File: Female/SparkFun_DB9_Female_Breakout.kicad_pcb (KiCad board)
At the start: 4 copper layers, 22.9 x 31 mm, 23 parts, among them J1 DB9-Female, J2 Conn_01x09

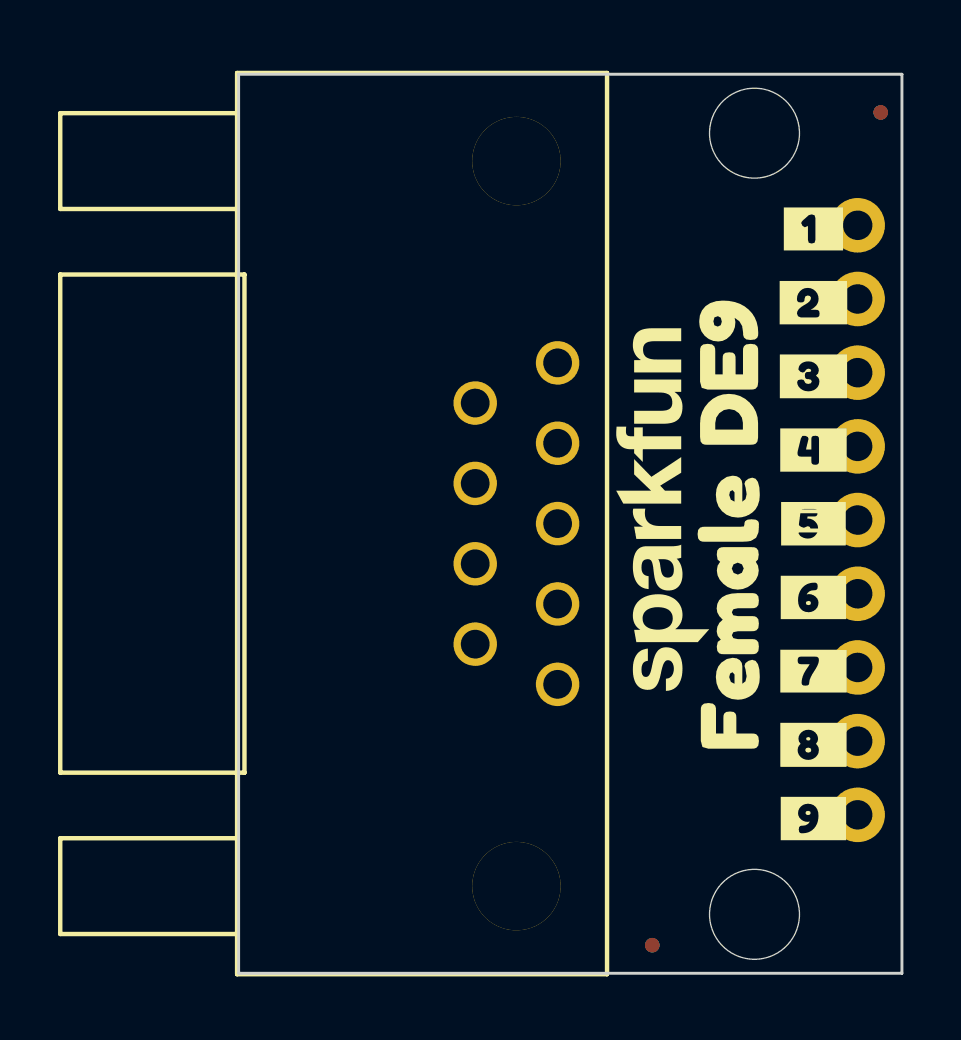
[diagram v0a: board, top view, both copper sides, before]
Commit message: Adds a male footprint for the DB9 and updates the affected board
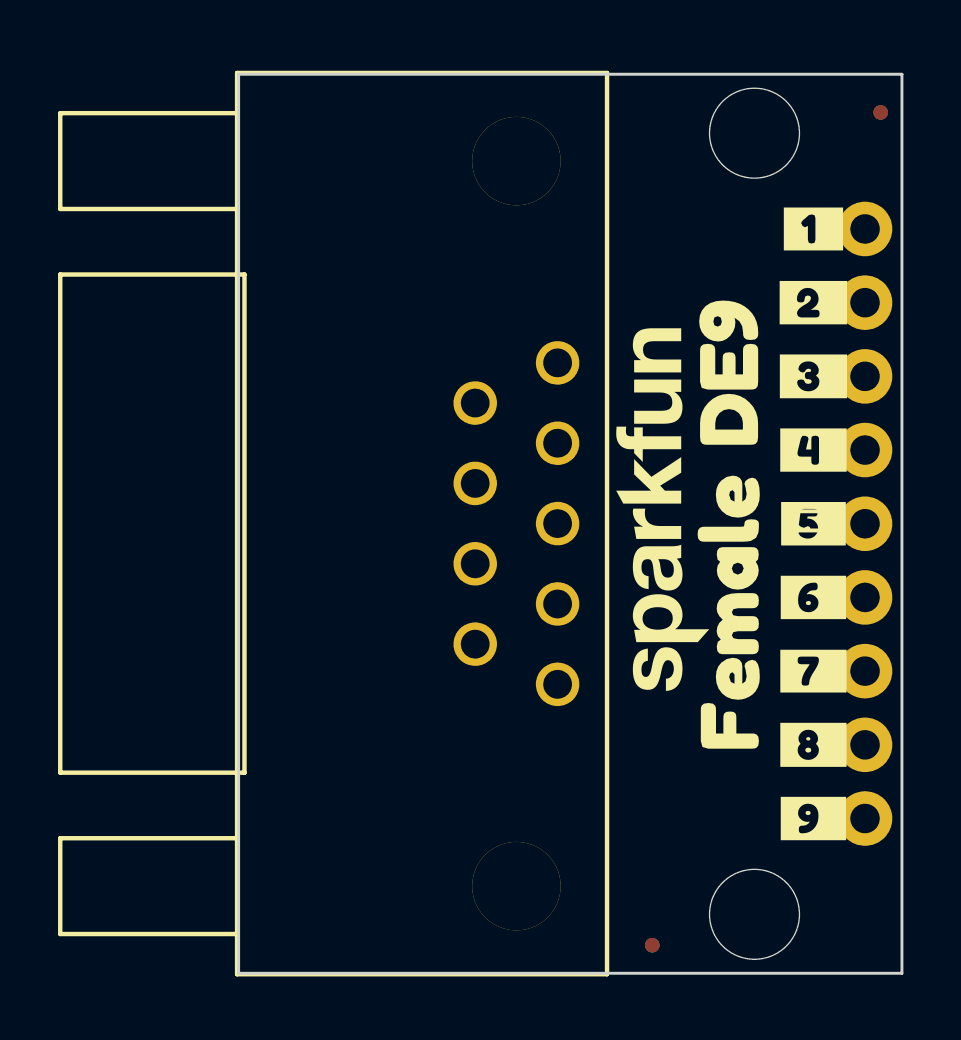
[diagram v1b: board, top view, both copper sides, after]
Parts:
- moved J2 20.2 mm to (131.1, 98.6), turned to -90 degrees
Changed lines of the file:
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@@
 	(footprint "SparkFun-Connector:1x09"
 		(layer "B.Cu")
-		(at 130.81 118.745 90)
+		(at 131.064 98.552 -90)
 		(tags "SparkFun")
 		(property "Reference" "J2"
@@
 		)
 		(property "Datasheet" ""
-			(at 0 0 270)
+			(at 0 0 90)
 			(unlocked yes)
 			(layer "B.Fab")
@@
 		)
 		(property "Description" "Basic 0.1\" PTH"
-			(at 0 0 270)
+			(at 0 0 90)
 			(unlocked yes)
 			(layer "B.Fab")
@@
 		(fp_poly
 			(pts
+				(xy -0.254 -0.254) (xy 0.254 -0.254) (xy 0.254 0.254) (xy -0.254 0.254)
+			)
+			(stroke
+				(width 0)
+				(type default)
+			)
+			(fill yes)
+			(layer "B.Fab")
+		)
+		(fp_poly
+			(pts
+				(xy 2.286 -0.254) (xy 2.794 -0.254) (xy 2.794 0.254) (xy 2.286 0.254)
+			)
+			(stroke
+				(width 0)
+				(type default)
+			)
+			(fill yes)
+			(layer "B.Fab")
+		)
+		(fp_poly
+			(pts
+				(xy 4.826 -0.254) (xy 5.334 -0.254) (xy 5.334 0.254) (xy 4.826 0.254)
+			)
+			(stroke
+				(width 0)
+				(type default)
+			)
+			(fill yes)
+			(layer "B.Fab")
+		)
+		(fp_poly
+			(pts
+				(xy 7.366 -0.254) (xy 7.874 -0.254) (xy 7.874 0.254) (xy 7.366 0.254)
+			)
+			(stroke
+				(width 0)
+				(type default)
+			)
+			(fill yes)
+			(layer "B.Fab")
+		)
+		(fp_poly
+			(pts
+				(xy 9.906 -0.254) (xy 10.414 -0.254) (xy 10.414 0.254) (xy 9.906 0.254)
+			)
+			(stroke
+				(width 0)
+				(type default)
+			)
+			(fill yes)
+			(layer "B.Fab")
+		)
+		(fp_poly
+			(pts
+				(xy 12.446 -0.254) (xy 12.954 -0.254) (xy 12.954 0.254) (xy 12.446 0.254)
+			)
+			(stroke
+				(width 0)
+				(type default)
+			)
+			(fill yes)
+			(layer "B.Fab")
+		)
+		(fp_poly
+			(pts
+				(xy 14.986 -0.254) (xy 15.494 -0.254) (xy 15.494 0.254) (xy 14.986 0.254)
+			)
+			(stroke
+				(width 0)
+				(type default)
+			)
+			(fill yes)
+			(layer "B.Fab")
+		)
+		(fp_poly
+			(pts
+				(xy 17.526 -0.254) (xy 18.034 -0.254) (xy 18.034 0.254) (xy 17.526 0.254)
+			)
+			(stroke
+				(width 0)
+				(type default)
+			)
+			(fill yes)
+			(layer "B.Fab")
+		)
+		(fp_poly
+			(pts
 				(xy 20.066 -0.254) (xy 20.574 -0.254) (xy 20.574 0.254) (xy 20.066 0.254)
 			)
@@
 			(layer "B.Fab")
 		)
-		(fp_poly
-			(pts
-				(xy 17.526 -0.254) (xy 18.034 -0.254) (xy 18.034 0.254) (xy 17.526 0.254)
-			)
-			(stroke
-				(width 0)
-				(type default)
-			)
-			(fill yes)
-			(layer "B.Fab")
-		)
-		(fp_poly
-			(pts
-				(xy 14.986 -0.254) (xy 15.494 -0.254) (xy 15.494 0.254) (xy 14.986 0.254)
-			)
-			(stroke
-				(width 0)
-				(type default)
-			)
-			(fill yes)
-			(layer "B.Fab")
-		)
-		(fp_poly
-			(pts
-				(xy 12.446 -0.254) (xy 12.954 -0.254) (xy 12.954 0.254) (xy 12.446 0.254)
-			)
-			(stroke
-				(width 0)
-				(type default)
-			)
-			(fill yes)
-			(layer "B.Fab")
-		)
-		(fp_poly
-			(pts
-				(xy 9.906 -0.254) (xy 10.414 -0.254) (xy 10.414 0.254) (xy 9.906 0.254)
-			)
-			(stroke
-				(width 0)
-				(type default)
-			)
-			(fill yes)
-			(layer "B.Fab")
-		)
-		(fp_poly
-			(pts
-				(xy 7.366 -0.254) (xy 7.874 -0.254) (xy 7.874 0.254) (xy 7.366 0.254)
-			)
-			(stroke
-				(width 0)
-				(type default)
-			)
-			(fill yes)
-			(layer "B.Fab")
-		)
-		(fp_poly
-			(pts
-				(xy 4.826 -0.254) (xy 5.334 -0.254) (xy 5.334 0.254) (xy 4.826 0.254)
-			)
-			(stroke
-				(width 0)
-				(type default)
-			)
-			(fill yes)
-			(layer "B.Fab")
-		)
-		(fp_poly
-			(pts
-				(xy 2.286 -0.254) (xy 2.794 -0.254) (xy 2.794 0.254) (xy 2.286 0.254)
-			)
-			(stroke
-				(width 0)
-				(type default)
-			)
-			(fill yes)
-			(layer "B.Fab")
-		)
-		(fp_poly
-			(pts
-				(xy -0.254 -0.254) (xy 0.254 -0.254) (xy 0.254 0.254) (xy -0.254 0.254)
-			)
-			(stroke
-				(width 0)
-				(type default)
-			)
-			(fill yes)
-			(layer "B.Fab")
-		)
 		(pad "1" thru_hole circle
-			(at 0 0)
+			(at 0 0 180)
 			(size 1.8796 1.8796)
 			(drill 1.016)
@@
 		)
 		(pad "2" thru_hole circle
-			(at 2.54 0)
+			(at 2.54 0 180)
 			(size 1.8796 1.8796)
 			(drill 1.016)
@@
 		)
 		(pad "3" thru_hole circle
-			(at 5.08 0)
+			(at 5.08 0 180)
 			(size 1.8796 1.8796)
 			(drill 1.016)
@@
 		)
 		(pad "4" thru_hole circle
-			(at 7.62 0)
+			(at 7.62 0 180)
 			(size 1.8796 1.8796)
 			(drill 1.016)
@@
 		)
 		(pad "5" thru_hole circle
-			(at 10.16 0)
+			(at 10.16 0 180)
 			(size 1.8796 1.8796)
 			(drill 1.016)
@@
 		)
 		(pad "6" thru_hole circle
-			(at 12.7 0)
+			(at 12.7 0 180)
 			(size 1.8796 1.8796)
 			(drill 1.016)
@@
 		)
 		(pad "7" thru_hole circle
-			(at 15.24 0)
+			(at 15.24 0 180)
 			(size 1.8796 1.8796)
 			(drill 1.016)
@@
 		)
 		(pad "8" thru_hole circle
-			(at 17.78 0)
+			(at 17.78 0 180)
 			(size 1.8796 1.8796)
 			(drill 1.016)
@@
 		)
 		(pad "9" thru_hole circle
-			(at 20.32 0)
-			(size 1.8796 1.8796)
-			(drill 1.016)
+			(at 20.32 0 180)
+			(size 1.8796 1.8796)
+			(drill 1.016)

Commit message: Adds gitignore, Fixes Female DB9 Connector, Adds more silk, Adds GND pins
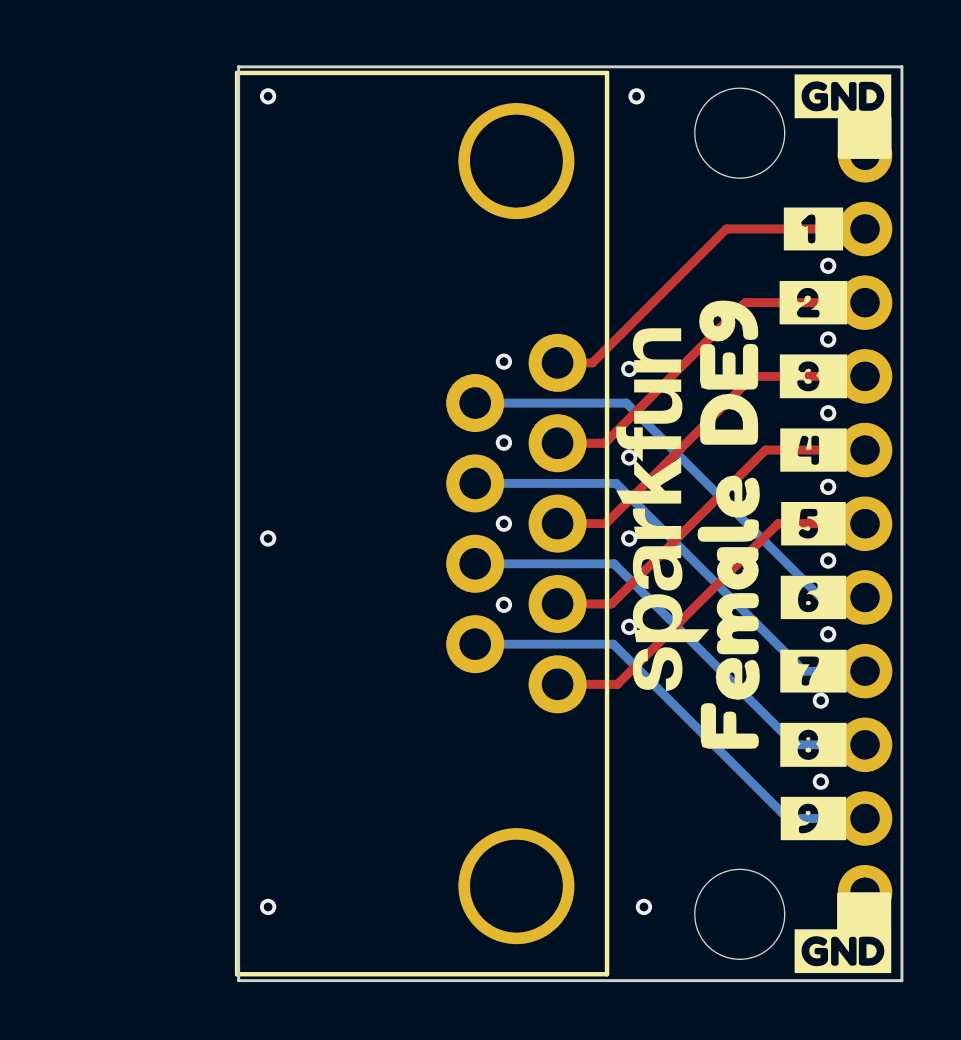
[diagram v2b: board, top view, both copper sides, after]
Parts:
- removed FID1, FID2, FID3, FID4: Fiducial_0.5mm, SparkFun-Aesthetic:Fiducial_0.5mm_Mask1mm
- removed the G*** at (113.8, 98.8)
- added G***: Flame, SparkFun-Aesthetic:SparkFun_Flame_6mm, B.Cu at (113.5, 97.0)
- added J3: Conn_01x01, SparkFun-Connector:1x01, F.Cu at (131.1, 121.4)
- added J4: Conn_01x01, SparkFun-Connector:1x01, F.Cu at (131.1, 96.0)
- added kibuzzard-67DDA384: G***, kibuzzard-67DDA384, B.Cu at (129.4, 98.5)
- added kibuzzard-67DDA391: G***, kibuzzard-67DDA391, B.Cu at (129.4, 101.1)
- added kibuzzard-67DDA399: G***, kibuzzard-67DDA399, B.Cu at (129.4, 103.6)
- added kibuzzard-67DDA3A2: G***, kibuzzard-67DDA3A2, B.Cu at (129.4, 106.1)
- added kibuzzard-67DDA3AA: G***, kibuzzard-67DDA3AA, B.Cu at (129.4, 108.7)
- added kibuzzard-67DDA3B0: G***, kibuzzard-67DDA3B0, B.Cu at (129.4, 111.2)
- added kibuzzard-67DDA3B8: G***, kibuzzard-67DDA3B8, B.Cu at (129.4, 113.8)
- added kibuzzard-67DDA3D5: G***, kibuzzard-67DDA3D5, B.Cu at (129.4, 116.3)
- added kibuzzard-67DDA3E0: G***, kibuzzard-67DDA3E0, B.Cu at (129.4, 118.8)
- added kibuzzard-67DDBC91: G***, kibuzzard-67DDBC91, F.Cu at (130.3, 94.0)
- added kibuzzard-67DDBC91: G***, kibuzzard-67DDBC91, F.Cu at (130.3, 123.4)
- added kibuzzard-67DDBC91: G***, kibuzzard-67DDBC91, B.Cu at (130.3, 123.4)
- added kibuzzard-67DDBC91: G***, kibuzzard-67DDBC91, B.Cu at (130.3, 94.0)
- added kibuzzard-67DDBDB0: G***, kibuzzard-67DDBDB0, B.Cu at (122.6, 105.8)
- added kibuzzard-67DDBDCA: G***, kibuzzard-67DDBDCA, B.Cu at (122.6, 103.0)
- added kibuzzard-67DDBDCE: G***, kibuzzard-67DDBDCE, B.Cu at (122.6, 108.8)
- added kibuzzard-67DDBDD2: G***, kibuzzard-67DDBDD2, B.Cu at (122.6, 111.6)
- added kibuzzard-67DDBDD7: G***, kibuzzard-67DDBDD7, B.Cu at (122.6, 114.3)
- added kibuzzard-67DDBDDC: G***, kibuzzard-67DDBDDC, B.Cu at (115.6, 113.0)
- added kibuzzard-67DDBDF0: G***, kibuzzard-67DDBDF0, B.Cu at (115.6, 107.3)
- added kibuzzard-67DDBDF6: G***, kibuzzard-67DDBDF6, B.Cu at (115.6, 110.2)
- added kibuzzard-67DDBDFC: G***, kibuzzard-67DDBDFC, B.Cu at (115.7, 104.4)
- J1: footprint DE9_Footprint:DB9 -> DE9_Footprint:DB9_Female
- moved ST1 0.51 mm to (126.7, 95.2)
- moved ST2 0.51 mm to (126.7, 122.2)
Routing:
- net /6: track 0.00 -> 16.2 mm
- net /7: track 0.00 -> 16.1 mm
- net /8: track 0.00 -> 16.0 mm
- net /9: track 0.00 -> 15.9 mm
- net /5: track 0.00 -> 12.9 mm
- net /4: track 0.00 -> 12.8 mm
- net /3: track 0.00 -> 12.7 mm
- net /2: track 0.00 -> 12.6 mm
- net /1: track 0.00 -> 12.5 mm
- net GND: vias 0 -> 21
- added copper zone on B.Cu, net GND
- added copper zone on F.Cu, net GND
- removed copper zone on B.Cu, net /9
- removed copper zone on F.Cu, net /9
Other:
- board size 22.9 x 31 mm -> 22.9 x 31.5 mm

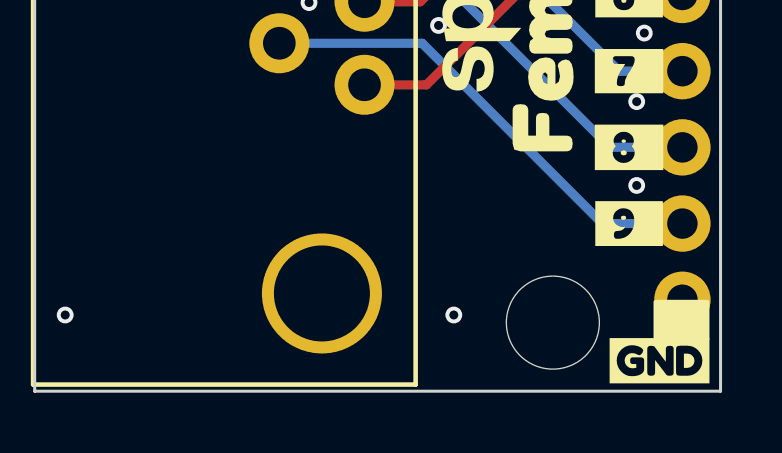
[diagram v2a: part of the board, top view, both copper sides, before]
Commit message: Adds some underbars to numbers, adds silk to bottom side on male DB9
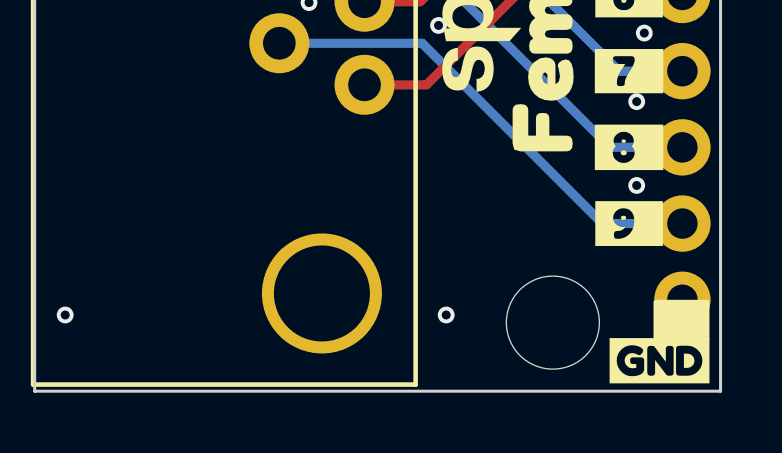
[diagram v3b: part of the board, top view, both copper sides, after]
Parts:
- moved kibuzzard-67DDBDFC 0.18 mm to (115.6, 104.4)
- moved kibuzzard-67DDA384 0.09 mm to (129.3, 98.6)
- moved kibuzzard-67DDA399 0.09 mm to (129.3, 103.6)
- moved kibuzzard-67DDA391 0.09 mm to (129.3, 101.1)
- moved kibuzzard-67DDA3A2 0.09 mm to (129.3, 106.2)
- moved kibuzzard-67DDA3AA 0.09 mm to (129.3, 108.7)
- moved kibuzzard-67DDA3B0 0.09 mm to (129.3, 111.3)
- moved kibuzzard-67DDA3B8 0.09 mm to (129.3, 113.8)
- moved kibuzzard-67DDA3D5 0.09 mm to (129.3, 116.3)
- moved kibuzzard-67DDA3E0 0.09 mm to (129.3, 118.9)

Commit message: Updates to the female DB9 footprint
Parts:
- moved J1 10.8 mm to (120.4, 108.7)
- moved G*** 0.92 mm to (112.8, 96.5)
- moved Ref** 0.91 mm to (114.0, 121.4)
- moved ST1 0.76 mm to (126.0, 95.2)
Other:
- copper layers 4 -> 2

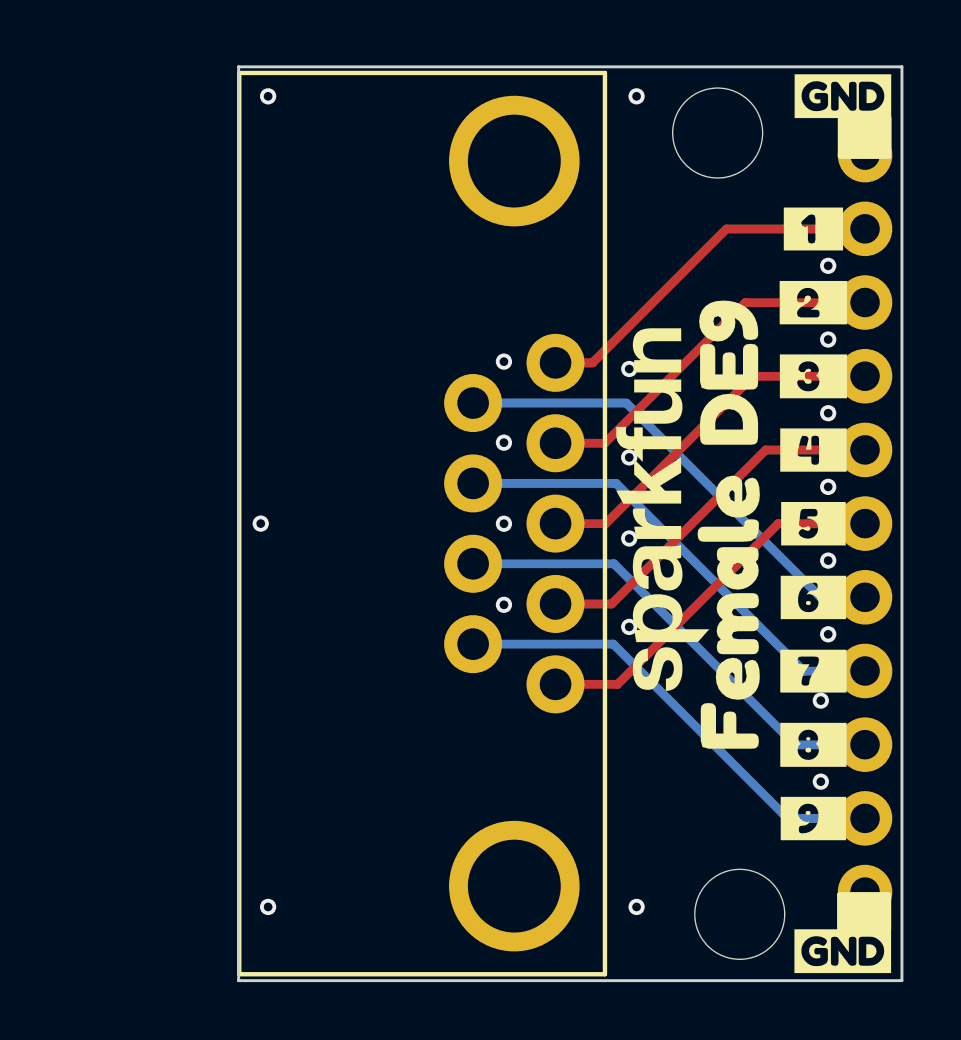
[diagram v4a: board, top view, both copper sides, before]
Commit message: Readjusts the design to have better symmetry and layout
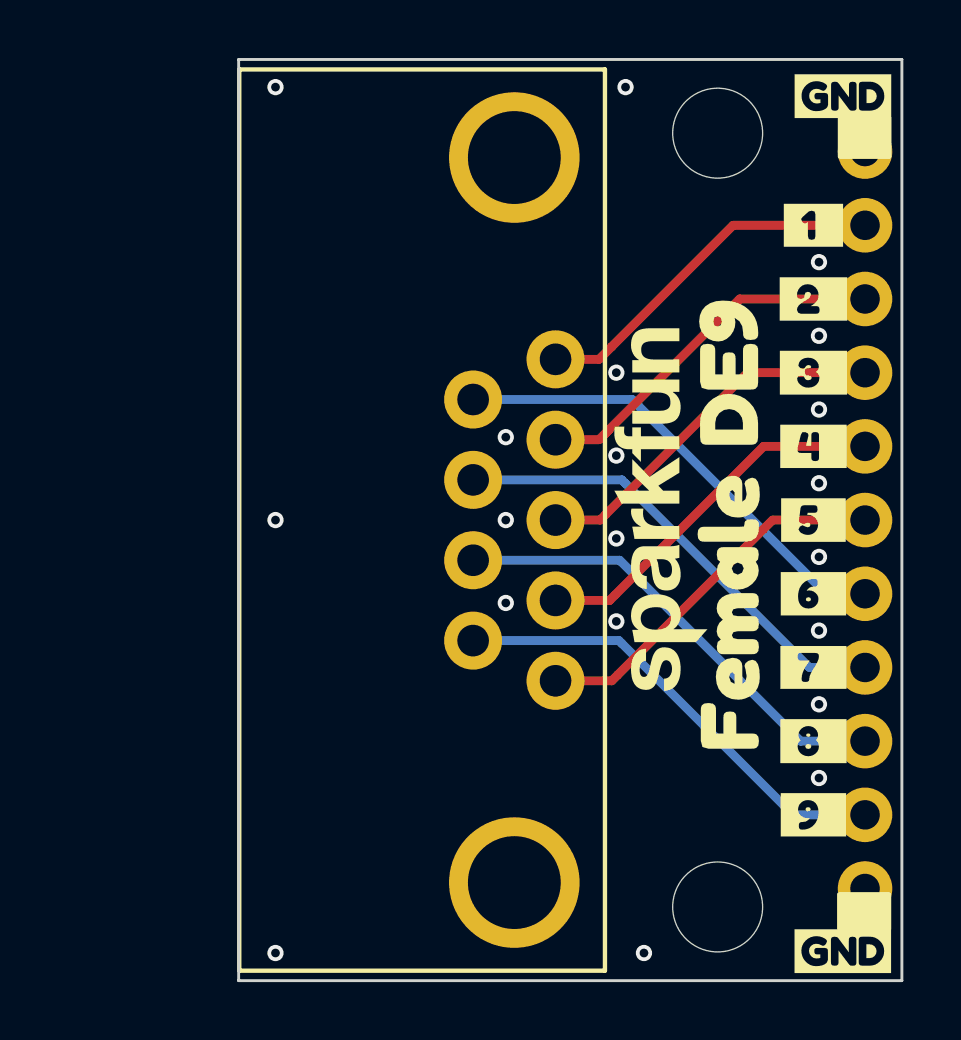
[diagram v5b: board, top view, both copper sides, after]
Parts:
- moved G*** 1.14 mm to (113.9, 96.5)
- moved ST2 0.80 mm to (126.0, 121.9)
- moved kibuzzard-67DDBDFC 0.27 mm to (115.8, 104.5)
- moved kibuzzard-67DDBDDC 0.25 mm to (115.8, 113.0)
- moved kibuzzard-67DDBDF0 0.25 mm to (115.8, 107.3)
- moved kibuzzard-67DDBDF6 0.25 mm to (115.8, 110.2)
- moved kibuzzard-67DDBDCE 0.18 mm to (122.6, 108.6)
- moved Ref** 0.18 mm to (113.9, 121.3)
- moved kibuzzard-67DDBDD2 0.14 mm to (122.6, 111.4)
- moved kibuzzard-67D49687 0.13 mm to (129.3, 98.4)
- moved kibuzzard-67D496C7 0.13 mm to (129.3, 103.5)
- moved kibuzzard-67D496D5 0.13 mm to (129.3, 108.6)
- moved kibuzzard-67DDA384 0.13 mm to (129.3, 98.4)
- moved kibuzzard-67DDA399 0.13 mm to (129.3, 103.5)
- moved kibuzzard-67DDA3AA 0.13 mm to (129.3, 108.6)
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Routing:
- net GND: vias 21 -> 15
- net (no net): vias 0 -> 5
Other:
- board size 22.9 x 31.5 mm -> 22.9 x 31.8 mm
